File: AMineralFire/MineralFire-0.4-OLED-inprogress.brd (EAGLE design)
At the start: 95.9 x 68.1 mm, 62 parts, among them IC3 LM358D, Q1 20MHz, T1 200mA/40V, U1 ATMEGA328P_TQFP, U2 7805

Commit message: Towards OLED
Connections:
- new net CS-DISP: U1.14
- new net DC-DISP: U1.27
- new net RST-DISP: U1.28
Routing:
- net GND: track 0.00 -> 419.6 mm, vias 0 -> 2
- net 5V: track 0.00 -> 270.5 mm, vias 0 -> 6
- net ENC2-G: track 0.00 -> 82.2 mm, vias 0 -> 2
- net ENC1_TERMA: track 0.00 -> 68.5 mm, vias 0 -> 2
- net BUT2: track 0.00 -> 63.9 mm, vias 0 -> 2
- net BUT3: track 0.00 -> 62.6 mm, vias 0 -> 3
- net ENC2-R: track 0.00 -> 61.4 mm, vias 0 -> 2
- net N$22: track 0.00 -> 61.1 mm, vias 0 -> 4
- net N$32: track 0.00 -> 58.4 mm
- net ENC1_TERMB: track 0.00 -> 56.0 mm, vias 0 -> 4
- net N$3: track 0.00 -> 53.8 mm, vias 0 -> 2
- net BUT1: track 0.00 -> 52.7 mm, vias 0 -> 2
- net ENC1-R: track 0.00 -> 51.8 mm, vias 0 -> 2
- net ENC2_TERMB: track 0.00 -> 48.9 mm, vias 0 -> 2
- net TRIGO: track 0.00 -> 47.6 mm, vias 0 -> 5
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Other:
- board text added: "V0.3 SMD OLED"
- board text removed: "V0.3 SMD"

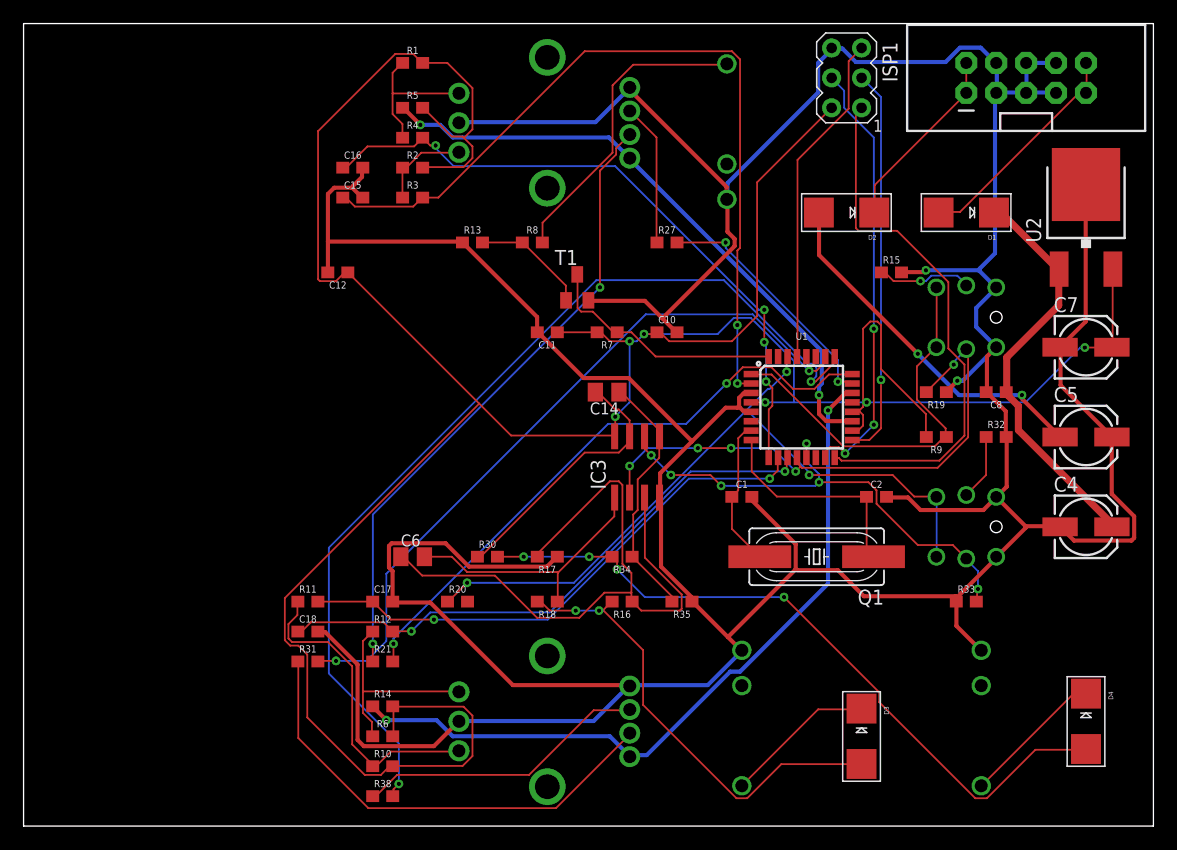
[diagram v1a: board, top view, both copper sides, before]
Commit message: trying connector for oled
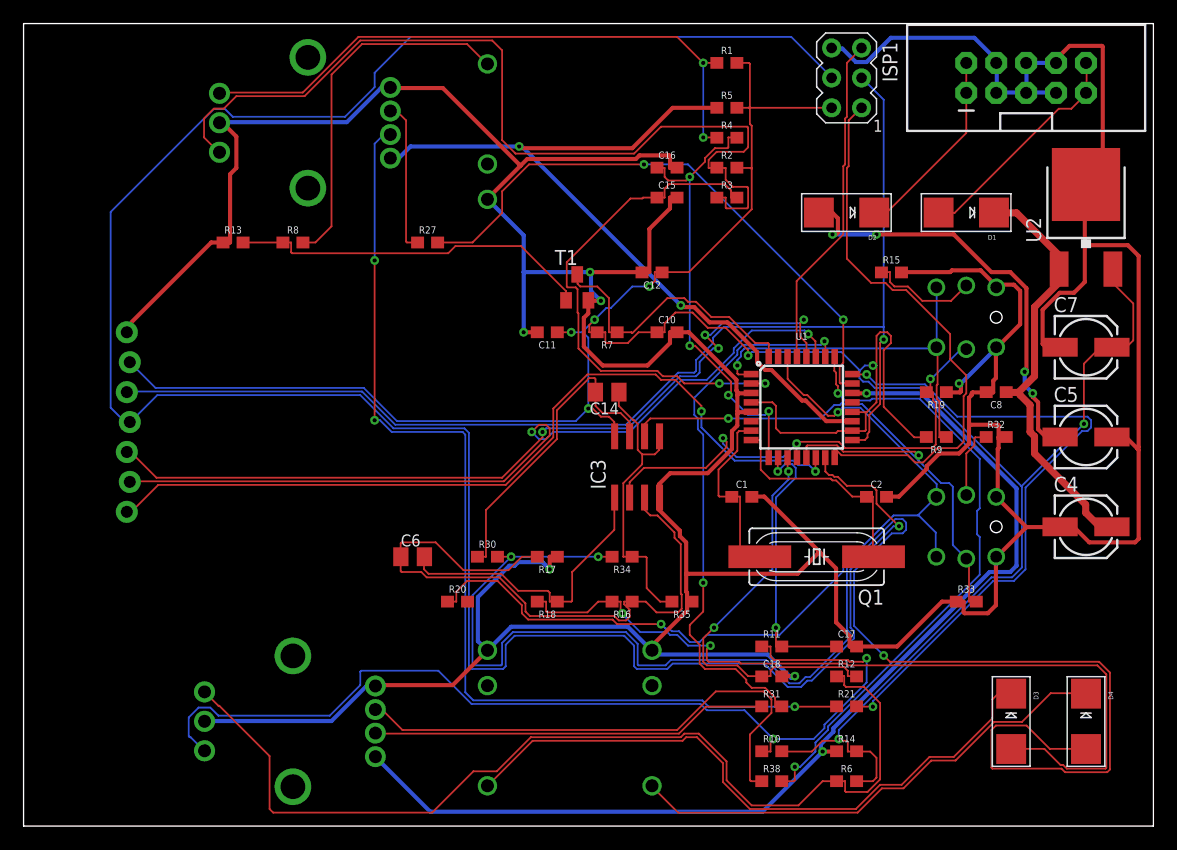
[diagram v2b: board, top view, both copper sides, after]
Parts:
- added J1: (no value), SparkFun-Connectors:1X07_LOCK
- moved C18 39.6 mm to (63.5, 12.7)
- moved R11 39.6 mm to (63.5, 15.2)
- moved R31 39.6 mm to (63.5, 10.2)
- moved C17 39.6 mm to (69.8, 15.2)
- moved R12 39.6 mm to (69.8, 12.7)
- moved R14 39.6 mm to (69.8, 6.35)
- moved R21 39.6 mm to (69.8, 10.2)
- moved R6 39.6 mm to (69.8, 3.81)
- moved R10 33.0 mm to (63.5, 6.35)
- moved R38 33.0 mm to (63.5, 3.81)
- moved TRIGOUT2 27.9 mm to (53.3, 8.42)
- moved C12 26.7 mm to (53.3, 47.0)
- moved C15 26.7 mm to (54.6, 53.3)
- moved C16 26.7 mm to (54.6, 55.9)
- moved R1 26.7 mm to (59.7, 64.8)
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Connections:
- net 5V: now also J1.2
- net CS-DISP: now also J1.7
- net DC-DISP: now also J1.6
- net GND: now also J1.1
- net MOSI: now also J1.4
- net RST-DISP: now also J1.5
- net SCK: now also J1.3
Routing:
- net MOSI: track 36.9 -> 201.3 mm, vias 3 -> 1
- net N$22: track 61.1 -> 137.5 mm, vias 4 -> 3
- net RST-DISP: track 0.00 -> 70.5 mm, vias 0 -> 4
- net CS-DISP: track 0.00 -> 70.4 mm, vias 0 -> 2
- net N$6: track 7.87 -> 77.9 mm
- net DC-DISP: track 0.00 -> 69.9 mm, vias 0 -> 2
- net SCK: track 33.3 -> 103.0 mm
- net N$28: track 17.8 -> 84.2 mm
- net N$27: track 26.9 -> 82.4 mm, vias 0 -> 2
- net N$74: track 12.9 -> 54.7 mm
- net N$12: track 12.7 -> 52.6 mm, vias 0 -> 2
- net N$3: track 53.8 -> 87.2 mm, vias 2 -> 3
- net N$34: track 39.5 -> 70.5 mm
- net N$23: track 12.1 -> 42.0 mm
- net ENC1-G: track 21.2 -> 50.3 mm
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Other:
- board text added: "CS-Disp"

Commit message: upadted
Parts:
- removed C7: 10u, rcl:153CLV-0505
- removed J1: (no value), SparkFun-Connectors:1X07_LOCK
- added C3: 10uF, rcl:153CLV-0505
- added IC1: 74AC32D, 74xx-eu:SO14
- added IC2: 74AC86D, 74xx-eu:SO14
- added JP1: (no value), Adafruit_1.3_128x64_OLED:MICROBUILDER_1X08_ROUND
- moved IC3 12.0 mm to (40.6, 34.3)
- moved C5 5.08 mm to (90.2, 27.9)
- moved C4 5.08 mm to (90.2, 20.3)
- moved R15 4.02 mm to (72.4, 43.2)
- moved U2 3.81 mm to (90.2, 48.3)
- moved T1 3.59 mm to (44.5, 48.3)
- moved U1 2.84 mm to (63.5, 36.8)
- moved ISP1 2.84 mm to (67.3, 62.2)
- moved POWER 1.80 mm to (83.8, 62.2)
- moved ENC1 1.17 mm to (23.0, 60.0)
- moved ENC2 0.70 mm to (23.0, 8.20)
- moved TRIGOUT2 0.40 mm to (53.0, 8.20)
- moved TRIGATEIN 0.29 mm to (39.4, 60.0), turned to 270 degrees
- moved TRIGOUT 0.22 mm to (39.4, 8.20)
- turned D1 to 270 degrees
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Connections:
- removed net B_TRIG: BUT.1, BUT.2, R9.1, U1.1
- new net BUT4: BUT.1, BUT.2, R9.1, U1.31
- new net ENC_INT: IC2.3, U1.1
- new net N$4: IC1.3, IC2.1
- new net N$5: IC1.6, IC2.2
- net 5V: now also C3.+, IC1.14, IC2.14, JP1.2; no longer C7.+, J1.2
- net CS-DISP: now also JP1.7; no longer J1.7
- net DC-DISP: now also JP1.6; no longer J1.6
- net ENC1_TERMA: now also IC1.1
- net ENC1_TERMB: now also IC1.2
- net ENC2_TERMA: now also IC1.4
- net ENC2_TERMB: now also IC1.5
- net GND: now also C3.-, IC1.7, IC2.7, JP1.1; no longer C7.-, J1.1
- net MOSI: now also JP1.4; no longer J1.4
- net RST-DISP: now also JP1.5; no longer J1.5
- net SCK: now also JP1.3; no longer J1.3
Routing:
- net MOSI: track 201.3 -> 100.3 mm, vias 1 -> 5
- net BUT4: track 0.00 -> 63.2 mm, vias 0 -> 8
- net N$22: track 137.5 -> 83.8 mm, vias 3 -> 2
- net ENC1_TERMB: track 38.4 -> 76.1 mm
- net ENC_INT: track 0.00 -> 35.9 mm, vias 0 -> 2
- net ENC2_TERMA: track 24.1 -> 59.7 mm, vias 2 -> 3
- net B_TRIG: track 33.4 -> 0.00 mm, vias 1 -> 0
- net MISO: track 47.5 -> 78.7 mm
- net 12V: track 36.4 -> 66.7 mm, vias 0 -> 2
- net ENC2_TERMB: track 35.1 -> 64.9 mm, vias 2 -> 3
- net TRIG1: track 53.1 -> 79.4 mm, vias 2 -> 0
- net N$3: track 87.2 -> 113.1 mm, vias 3 -> 1
- net N$6: track 77.9 -> 52.7 mm, vias 0 -> 3
- net ENC1-R: track 56.6 -> 31.7 mm
- net ENC1_TERMA: track 44.9 -> 66.1 mm, vias 2 -> 4
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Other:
- board text added: "V0.4 SMD OLED"
- board text removed: "V0.3 SMD OLED"
